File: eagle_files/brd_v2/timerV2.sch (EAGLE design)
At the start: 42 parts, among them IC6 DS1307, U1 ATMEGA328P

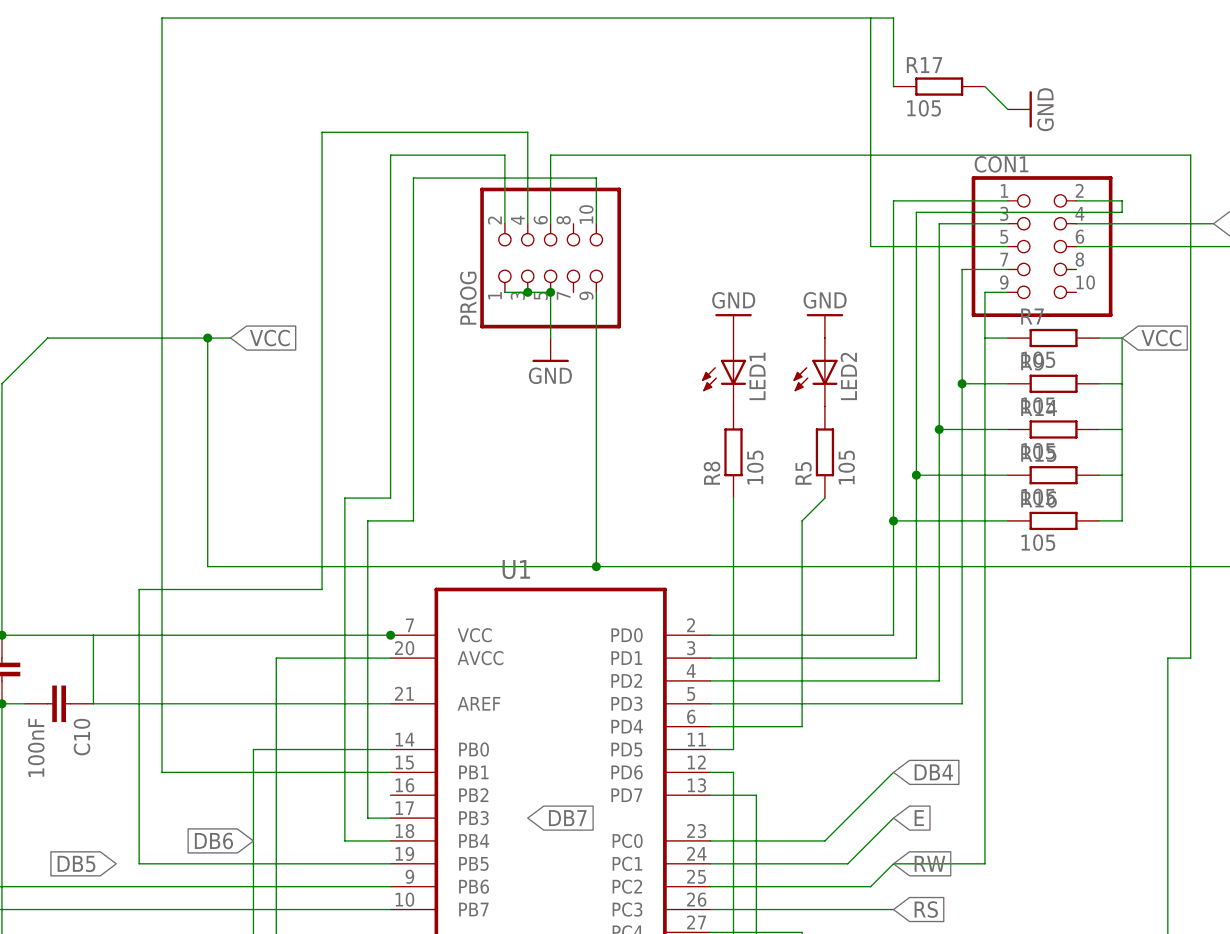
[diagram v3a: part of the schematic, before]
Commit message: changed layout
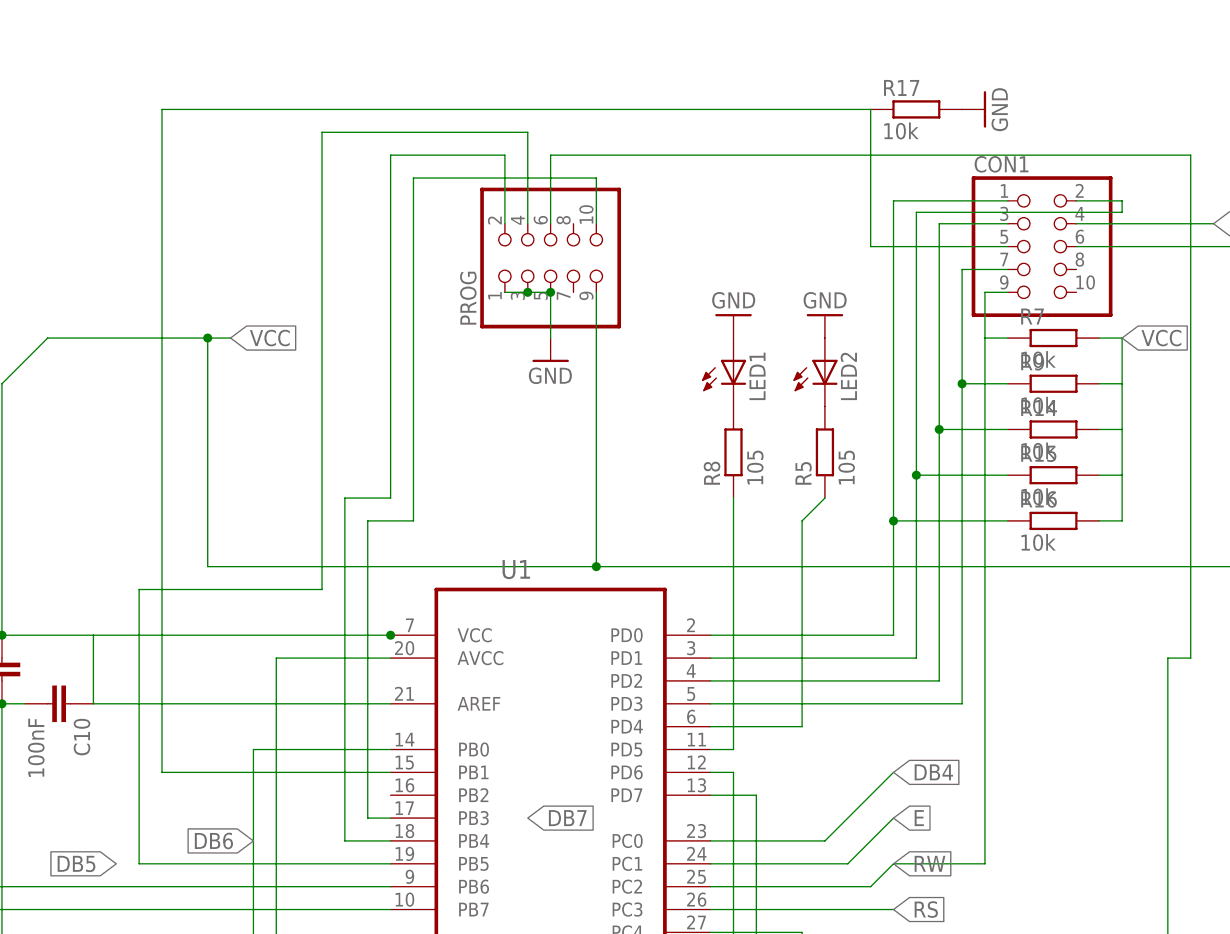
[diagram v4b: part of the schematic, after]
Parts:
- R14, R15, R16, R17, R7, R9: value 105 -> 10k
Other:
- moved on the sheet: R17
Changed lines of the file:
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@@
 <?xml version="1.0" encoding="utf-8"?>
 <!DOCTYPE eagle SYSTEM "eagle.dtd">
-<eagle version="6.4">
+<eagle version="6.5.0">
 <drawing>
 <settings>
@@
 <part name="R8" library="eagle-ltspice" deviceset="R" device="R0603" value="105"/>
 <part name="CON1" library="pinhead" deviceset="PINHD-2X5" device=""/>
-<part name="R7" library="eagle-ltspice" deviceset="R" device="R0603" value="105"/>
-<part name="R9" library="eagle-ltspice" deviceset="R" device="R0603" value="105"/>
-<part name="R14" library="eagle-ltspice" deviceset="R" device="R0603" value="105"/>
-<part name="R15" library="eagle-ltspice" deviceset="R" device="R0603" value="105"/>
-<part name="R16" library="eagle-ltspice" deviceset="R" device="R0603" value="105"/>
-<part name="R17" library="eagle-ltspice" deviceset="R" device="R0603" value="105"/>
+<part name="R7" library="eagle-ltspice" deviceset="R" device="R0603" value="10k"/>
+<part name="R9" library="eagle-ltspice" deviceset="R" device="R0603" value="10k"/>
+<part name="R14" library="eagle-ltspice" deviceset="R" device="R0603" value="10k"/>
+<part name="R15" library="eagle-ltspice" deviceset="R" device="R0603" value="10k"/>
+<part name="R16" library="eagle-ltspice" deviceset="R" device="R0603" value="10k"/>
+<part name="R17" library="eagle-ltspice" deviceset="R" device="R0603" value="10k"/>
 <part name="GND10" library="supply1" deviceset="GND" device=""/>
 </parts>
@@
 <instance part="R15" gate="G$1" x="-7.62" y="129.54"/>
 <instance part="R16" gate="G$1" x="-7.62" y="124.46"/>
-<instance part="R17" gate="G$1" x="-20.32" y="172.72"/>
-<instance part="GND10" gate="1" x="-10.16" y="170.18" rot="R90"/>
+<instance part="R17" gate="G$1" x="-22.86" y="170.18"/>
+<instance part="GND10" gate="1" x="-15.24" y="170.18" rot="R90"/>
 </instances>
 <busses>
@@
 <pinref part="R17" gate="G$1" pin="2"/>
 <pinref part="GND10" gate="1" pin="GND"/>
-<wire x1="-12.7" y1="170.18" x2="-15.24" y2="172.72" width="0.1524" layer="91"/>
 </segment>
 </net>
@@
 <pinref part="U1" gate="A" pin="PB1"/>
 <wire x1="-106.68" y1="96.52" x2="-81.28" y2="96.52" width="0.1524" layer="91"/>
-<wire x1="-106.68" y1="96.52" x2="-106.68" y2="180.34" width="0.1524" layer="91"/>
-<wire x1="-106.68" y1="180.34" x2="-27.94" y2="180.34" width="0.1524" layer="91"/>
-<wire x1="-27.94" y1="180.34" x2="-27.94" y2="154.94" width="0.1524" layer="91"/>
+<wire x1="-106.68" y1="96.52" x2="-106.68" y2="170.18" width="0.1524" layer="91"/>
+<wire x1="-106.68" y1="170.18" x2="-27.94" y2="170.18" width="0.1524" layer="91"/>
+<wire x1="-27.94" y1="170.18" x2="-27.94" y2="154.94" width="0.1524" layer="91"/>
 <wire x1="-27.94" y1="154.94" x2="-12.7" y2="154.94" width="0.1524" layer="91"/>
 <pinref part="CON1" gate="A" pin="5"/>
 <pinref part="R17" gate="G$1" pin="1"/>
-<wire x1="-25.4" y1="172.72" x2="-25.4" y2="180.34" width="0.1524" layer="91"/>
-<wire x1="-25.4" y1="180.34" x2="-27.94" y2="180.34" width="0.1524" layer="91"/>
 </segment>
 </net>
@@
 </sheet>
 </sheets>
-<errors>
-</errors>
 </schematic>
 </drawing>

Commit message: Schematic cleaned up
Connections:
- net N$3 renamed POWER_SWITCH
- new net N$10: JP1.7, U$2.DB0
- new net N$16: JP1.8, U$2.DB1
- new net N$18: JP1.9, U$2.DB2
- new net N$19: JP1.10, U$2.DB3
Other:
- moved on the sheet: C1, C10, C2, C3, C4, C5, C6, C7, C8, CON1, IC6, JP1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
